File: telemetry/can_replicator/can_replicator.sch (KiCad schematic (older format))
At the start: 34 parts, among them J1 CONN_02X03, J2 MM_M_VT_20, U1 MCP2561-E_SN, U2 ATMEGA16M1, U3 USB_MicroB, U4 FT232RL, Y1 Crystal_SMD

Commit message: fix: fixes based on review checklist
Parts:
- added D7: BAT400D-7-F, footprints:SOT-23-3_OEM, symbol formula:BAT400D-7-F
- added F1: F_500mA_16V, footprints:Fuse_1210, symbol formula:F_500mA_16V
- added U5, U6: R_500, footprints:R_0805_OEM, symbol formula:R_500
- C1, C2: symbol template-rescue:C_0.1uF-formula -> formula:C_0.1uF
- C3: symbol template-rescue:C_100pF-formula -> formula:C_100pF
- C4, C5: symbol template-rescue:C_30pF-formula -> formula:C_30pF
- J1: symbol template-rescue:CONN_02X03-formula -> formula:CONN_02X03
- R1: symbol template-rescue:R_100-formula -> formula:R_100
- R3: symbol template-rescue:R_10K-formula -> formula:R_10K
- U1: symbol template-rescue:MCP2561-E_SN-formula -> formula:MCP2561-E_SN
- Y1: symbol template-rescue:Crystal_SMD-formula -> formula:Crystal_SMD
- gave numbers to parts that had none: 1
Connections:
- net labels added: +5V
- net labels removed: VCC
- wire segments 95 -> 102
- no-connect marks 30 -> 32
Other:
- note added: "+4.4V - +5.25V"
- moved on the sheet: C6, C7, C8, C9, D8, TP2, U4

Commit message: fix: cleanup schematic based on DR feedback
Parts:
- removed J2: MM_M_VT_20, footprints:micromatch_female_vert_20, symbol formula:MM_M_VT_20
- added J?: MM_M_VT_20, footprints:micromatch_female_ra_20, symbol formula:MM_M_VT_20
- renumbered U5 to R10, U6 to R11
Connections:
- net CAN_+: now also J?.3
- net CAN_-: now also J?.4
- net GND: now also J?.1, J?.10, J?.11, J?.12, J?.13, J?.14, J?.15, J?.16, J?.17, J?.18, J?.19, J?.20, J?.5, J?.6, J?.7, J?.8, J?.9
- net USB_RXD renamed UART_RXD
- net USB_TXD renamed UART_TXD
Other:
- note added: "CONNECTOR"
- moved on the sheet: C6, D1, D2, D3, D4, D5, D6, J1, R4, R5, R6, R7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

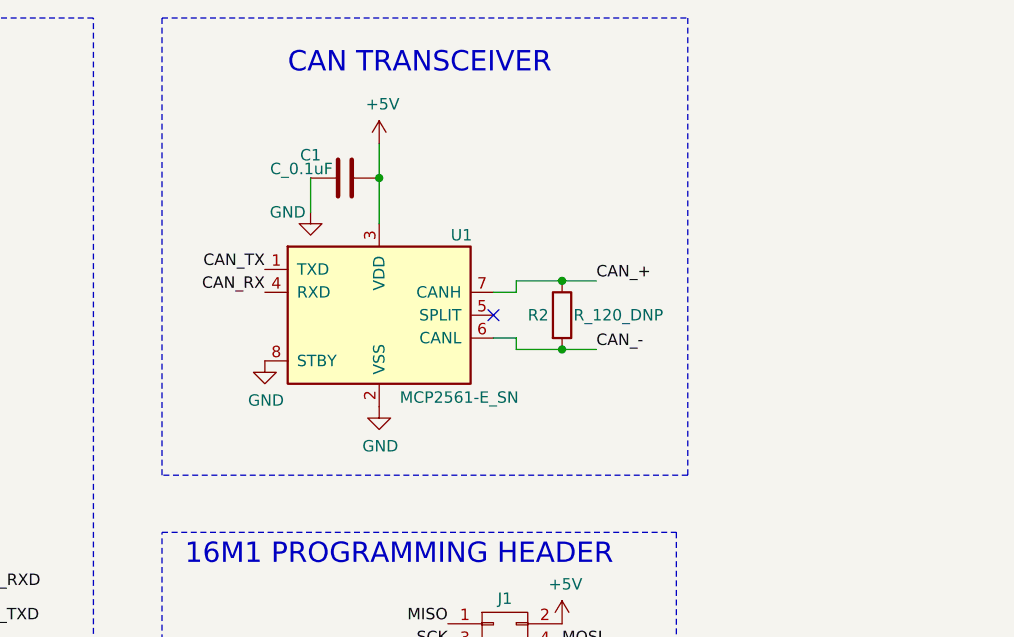
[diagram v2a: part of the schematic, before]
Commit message: feat: add terminating resistors for CAN bus with jumpers
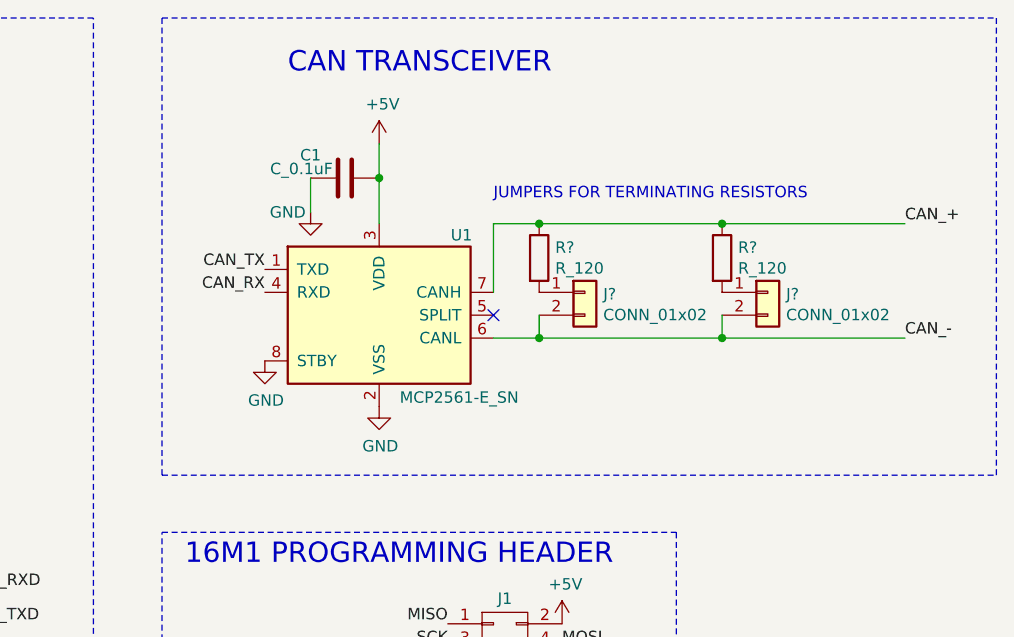
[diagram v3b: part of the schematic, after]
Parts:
- removed R2: R_120_DNP, footprints:R_0805_OEM, symbol formula:R_120_DNP
- added J? (x2): CONN_01x02, Connector_PinHeader_2.54mm:PinHeader_1x02_P2.54mm_Vertical, symbol formula:CONN_01x02
- added R? (x2): R_120, footprints:R_0805_OEM, symbol formula:R_120
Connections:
- net CAN_+: now also R?.1, R?.1
- net CAN_-: now also J?.2 (Pin_2), J?.2 (Pin_2)
- new net: J?.1 (Pin_1), R?.2 (x2)
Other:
- note added: "JUMPERS FOR TERMINATING RESISTORS"
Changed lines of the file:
@@
 Text Label 5850 2200 2    50   ~ 0
 CAN_RX
-Text Label 7300 2150 0    50   ~ 0
+Text Label 8650 1900 0    50   ~ 0
 CAN_+
-Text Label 7300 2450 0    50   ~ 0
+Text Label 8650 2400 0    50   ~ 0
 CAN_-
 Text Notes 2550 1250 0    89   ~ 0
@@
 Wire Wire Line
 	6350 1700 6350 1550
-Wire Wire Line
-	6850 2200 6950 2200
-Wire Wire Line
-	6950 2200 6950 2150
-Wire Wire Line
-	6950 2400 6950 2450
-Wire Wire Line
-	6850 2400 6950 2400
 Text Notes 1800 6050 0    89   ~ 0
 USB + POWER
@@
 	5100 1000 850  1000
 Wire Notes Line
-	5400 1000 7700 1000
-Wire Notes Line
-	7700 1000 7700 3000
-Wire Notes Line
-	7700 3000 5400 3000
+	9050 1000 9050 3000
 Wire Notes Line
 	5400 3000 5400 1000
@@
 	1    0    0    -1
 $EndComp
-Wire Wire Line
-	6950 2150 7150 2150
-Wire Wire Line
-	6950 2450 7150 2450
-$Comp
-L formula:R_120_DNP R2
-U 1 1 5FB3CE18
-P 7150 2300
-F 0 "R2" H 7000 2300 50  0000 L CNN
-F 1 "R_120_DNP" H 7200 2300 50  0000 L CNN
-F 2 "footprints:R_0805_OEM" H 5950 2450 50  0001 L CNN
-F 3 "https://www.mouser.com/datasheet/2/315/AOA0000C304-1149620.pdf" H 5950 2750 50  0001 L CNN
-F 4 "DK" H 7150 2300 60  0001 C CNN "MFN"
-F 5 "667-ERJ-6ENF1200V" H 5950 2550 60  0001 L CNN "MPN"
-F 6 "https://www.mouser.com/ProductDetail/Panasonic-Industrial-Devices/ERJ-6ENF1200V?qs=sGAEpiMZZMvdGkrng054t8AJgcdMkx7x%252bFQnctTMUmU%3d" H 5950 2650 60  0001 L CNN "PurchasingLink"
-	1    7150 2300
-	1    0    0    -1
-$EndComp
-Connection ~ 7150 2150
-Wire Wire Line
-	7150 2150 7300 2150
-Connection ~ 7150 2450
-Wire Wire Line
-	7150 2450 7300 2450
 NoConn ~ 1100 7550
 NoConn ~ 3950 3750
@@
 Text Label 4500 3650 0    50   ~ 0
 UART_TXD
+$Comp
+L formula:CONN_01x02 J?
+U 1 1 604765A9
+P 7250 2200
+F 0 "J?" H 7330 2192 50  0000 L CNN
+F 1 "CONN_01x02" H 7330 2101 50  0000 L CNN
+F 2 "Connector_PinHeader_2.54mm:PinHeader_1x02_P2.54mm_Vertical" H 7150 2200 50  0001 C CNN
+F 3 "https://katalog.we-online.de/em/datasheet/6130xx11121.pdf" H 7250 2300 50  0001 C CNN
+F 4 "DK" H 7350 2400 50  0001 C CNN "MFN"
+F 5 "732-5315-ND" H 7450 2500 50  0001 C CNN "MPN"
+	1    7250 2200
+	1    0    0    -1
+$EndComp
+Wire Wire Line
+	6850 2400 7050 2400
+Wire Wire Line
+	7050 2300 7050 2400
+Connection ~ 7050 2400
+Wire Wire Line
+	7050 2400 7850 2400
+$Comp
+L formula:R_120 R?
+U 1 1 604A0174
+P 7050 2050
+F 0 "R?" H 7120 2096 50  0000 L CNN
+F 1 "R_120" H 7120 2005 50  0000 L CNN
+F 2 "footprints:R_0805_OEM" H 5850 2200 50  0001 L CNN
+F 3 "https://www.mouser.com/datasheet/2/315/AOA0000C304-1149620.pdf" H 5850 2500 50  0001 L CNN
+F 4 "DK" H 7050 2050 60  0001 C CNN "MFN"
+F 5 "667-ERJ-6ENF1200V" H 5850 2300 60  0001 L CNN "MPN"
+F 6 "https://www.mouser.com/ProductDetail/Panasonic-Industrial-Devices/ERJ-6ENF1200V?qs=sGAEpiMZZMvdGkrng054t8AJgcdMkx7x%252bFQnctTMUmU%3d" H 5850 2400 60  0001 L CNN "PurchasingLink"
+	1    7050 2050
+	1    0    0    -1
+$EndComp
+Wire Wire Line
+	6850 2200 6850 1900
+Wire Wire Line
+	6850 1900 7050 1900
+Connection ~ 7050 1900
+Wire Wire Line
+	7050 1900 7850 1900
+$Comp
+L formula:CONN_01x02 J?
+U 1 1 604B1E63
+P 8050 2200
+F 0 "J?" H 8130 2192 50  0000 L CNN
+F 1 "CONN_01x02" H 8130 2101 50  0000 L CNN
+F 2 "Connector_PinHeader_2.54mm:PinHeader_1x02_P2.54mm_Vertical" H 7950 2200 50  0001 C CNN
+F 3 "https://katalog.we-online.de/em/datasheet/6130xx11121.pdf" H 8050 2300 50  0001 C CNN
+F 4 "DK" H 8150 2400 50  0001 C CNN "MFN"
+F 5 "732-5315-ND" H 8250 2500 50  0001 C CNN "MPN"
+	1    8050 2200
+	1    0    0    -1
+$EndComp
+Wire Wire Line
+	7850 2300 7850 2400
+$Comp
+L formula:R_120 R?
+U 1 1 604B2391
+P 7850 2050
+F 0 "R?" H 7920 2096 50  0000 L CNN
+F 1 "R_120" H 7920 2005 50  0000 L CNN
+F 2 "footprints:R_0805_OEM" H 6650 2200 50  0001 L CNN
+F 3 "https://www.mouser.com/datasheet/2/315/AOA0000C304-1149620.pdf" H 6650 2500 50  0001 L CNN
+F 4 "DK" H 7850 2050 60  0001 C CNN "MFN"
+F 5 "667-ERJ-6ENF1200V" H 6650 2300 60  0001 L CNN "MPN"
+F 6 "https://www.mouser.com/ProductDetail/Panasonic-Industrial-Devices/ERJ-6ENF1200V?qs=sGAEpiMZZMvdGkrng054t8AJgcdMkx7x%252bFQnctTMUmU%3d" H 6650 2400 60  0001 L CNN "PurchasingLink"
+	1    7850 2050
+	1    0    0    -1
+$EndComp
+Connection ~ 7850 1900
+Connection ~ 7850 2400
+Wire Wire Line
+	7850 2400 8650 2400
+Wire Wire Line
+	7850 1900 8650 1900
+Wire Notes Line
+	5400 3000 9050 3000
+Wire Notes Line
+	5400 1000 9050 1000
+Text Notes 6850 1800 0    50   ~ 0
+JUMPERS FOR TERMINATING RESISTORS
 $EndSCHEMATC

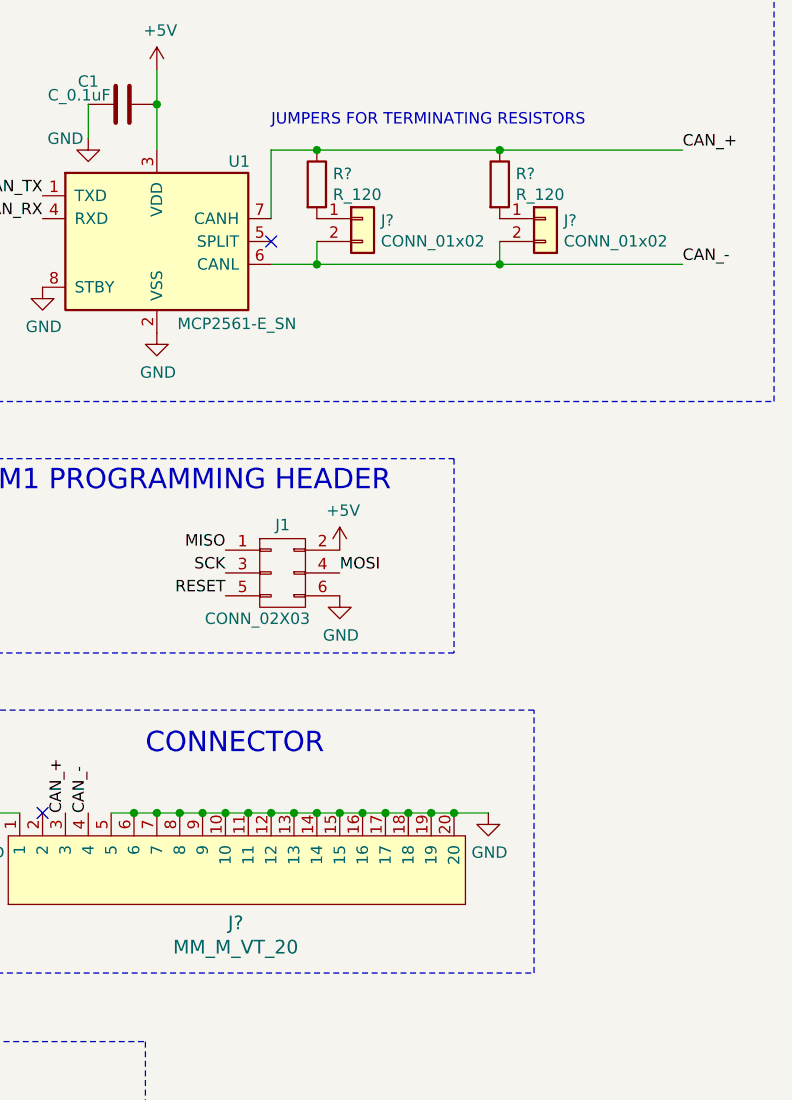
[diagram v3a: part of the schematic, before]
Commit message: chore: annotate symbols and assign footprints
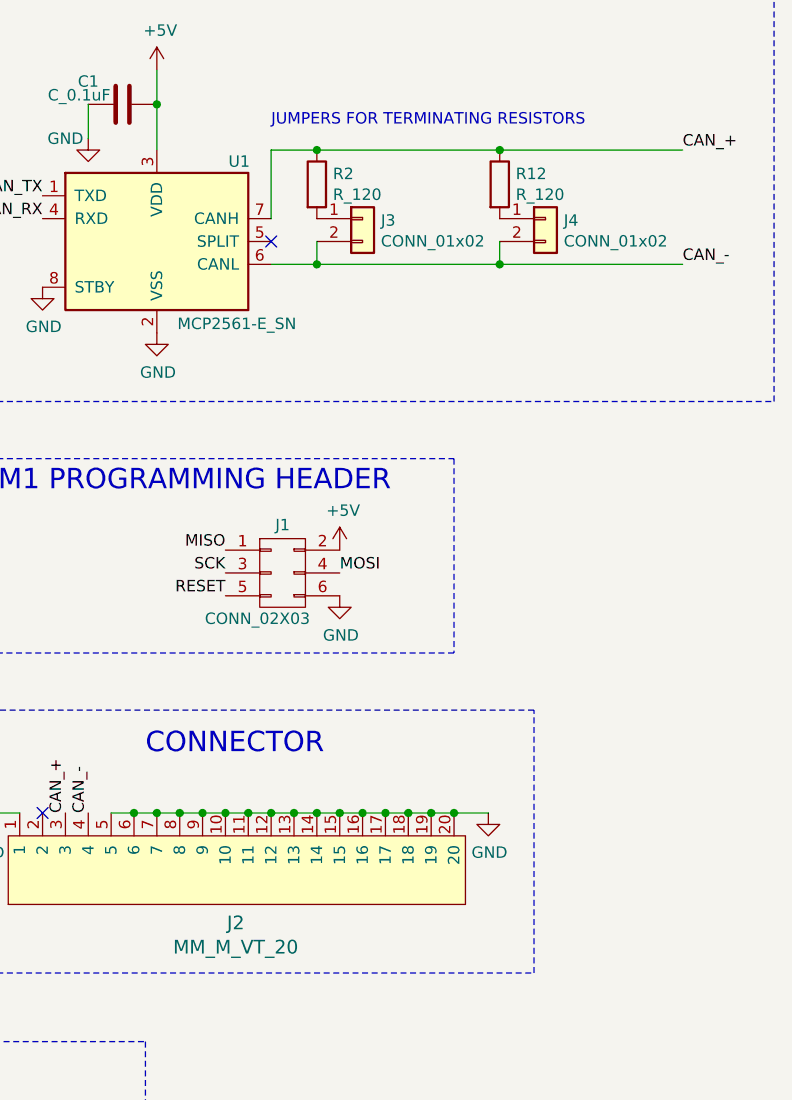
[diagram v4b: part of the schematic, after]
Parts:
- gave numbers to parts that had none: 5
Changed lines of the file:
@@
 STATUS LEDS
 $Comp
-L formula:MM_M_VT_20 J?
+L formula:MM_M_VT_20 J2
 U 1 1 60394CE9
 P 6850 4950
-F 0 "J?" V 6519 5105 60  0000 C CNN
+F 0 "J2" V 6519 5105 60  0000 C CNN
 F 1 "MM_M_VT_20" V 6413 5105 60  0000 C CNN
 F 2 "footprints:micromatch_female_ra_20" H 6650 6050 60  0001 C CNN
@@
 	7650 4800 7800 4800
 $Comp
-L power:GND #PWR?
+L power:GND #PWR020
 U 1 1 6039EEAA
 P 7800 4800
-F 0 "#PWR?" H 7800 4550 50  0001 C CNN
+F 0 "#PWR020" H 7800 4550 50  0001 C CNN
 F 1 "GND" H 7805 4627 50  0000 C CNN
 F 2 "" H 7800 4800 50  0001 C CNN
@@
 $EndComp
 $Comp
-L power:GND #PWR?
+L power:GND #PWR019
 U 1 1 6039FA95
 P 5600 4800
-F 0 "#PWR?" H 5600 4550 50  0001 C CNN
+F 0 "#PWR019" H 5600 4550 50  0001 C CNN
 F 1 "GND" H 5605 4627 50  0000 C CNN
 F 2 "" H 5600 4800 50  0001 C CNN
@@
 UART_TXD
 $Comp
-L formula:CONN_01x02 J?
+L formula:CONN_01x02 J3
 U 1 1 604765A9
 P 7250 2200
-F 0 "J?" H 7330 2192 50  0000 L CNN
+F 0 "J3" H 7330 2192 50  0000 L CNN
 F 1 "CONN_01x02" H 7330 2101 50  0000 L CNN
 F 2 "Connector_PinHeader_2.54mm:PinHeader_1x02_P2.54mm_Vertical" H 7150 2200 50  0001 C CNN
@@
 	7050 2400 7850 2400
 $Comp
-L formula:R_120 R?
+L formula:R_120 R2
 U 1 1 604A0174
 P 7050 2050
-F 0 "R?" H 7120 2096 50  0000 L CNN
+F 0 "R2" H 7120 2096 50  0000 L CNN
 F 1 "R_120" H 7120 2005 50  0000 L CNN
 F 2 "footprints:R_0805_OEM" H 5850 2200 50  0001 L CNN
@@
 	7050 1900 7850 1900
 $Comp
-L formula:CONN_01x02 J?
+L formula:CONN_01x02 J4
 U 1 1 604B1E63
 P 8050 2200
-F 0 "J?" H 8130 2192 50  0000 L CNN
+F 0 "J4" H 8130 2192 50  0000 L CNN
 F 1 "CONN_01x02" H 8130 2101 50  0000 L CNN
 F 2 "Connector_PinHeader_2.54mm:PinHeader_1x02_P2.54mm_Vertical" H 7950 2200 50  0001 C CNN
@@
 	7850 2300 7850 2400
 $Comp
-L formula:R_120 R?
+L formula:R_120 R12
 U 1 1 604B2391
 P 7850 2050
-F 0 "R?" H 7920 2096 50  0000 L CNN
+F 0 "R12" H 7920 2096 50  0000 L CNN
 F 1 "R_120" H 7920 2005 50  0000 L CNN
 F 2 "footprints:R_0805_OEM" H 6650 2200 50  0001 L CNN

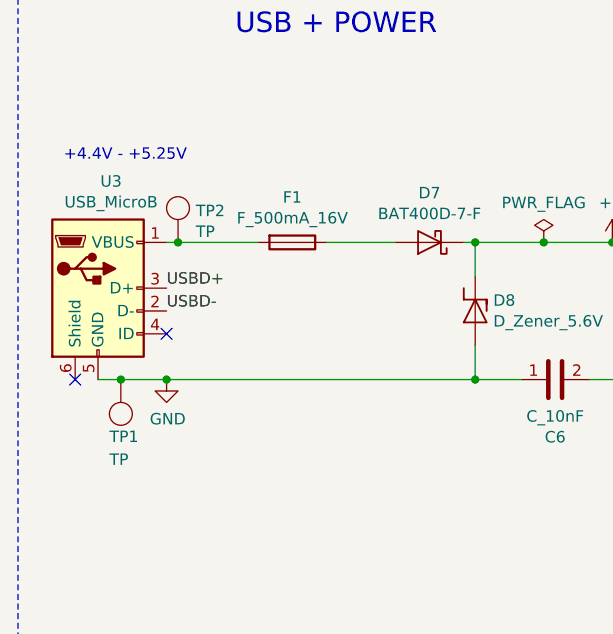
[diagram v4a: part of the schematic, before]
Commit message: fix: replace test points with SMD
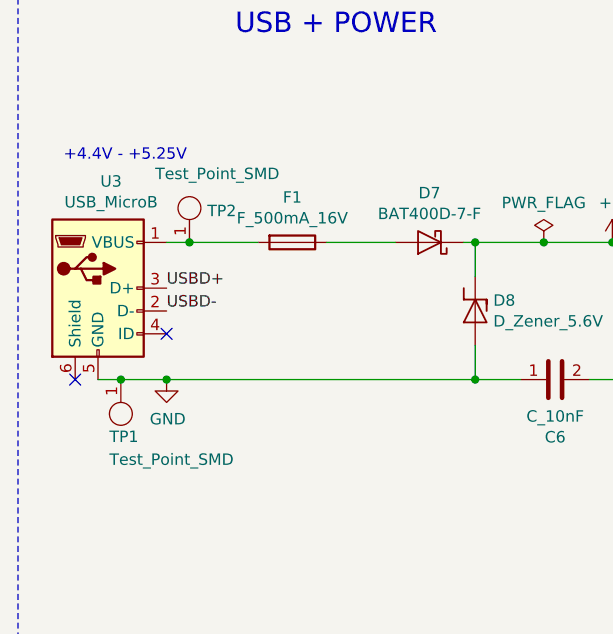
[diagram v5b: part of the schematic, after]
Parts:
- removed TP1, TP2: TP, footprints:tp_1.6mm, symbol formula:TP
- added TP1, TP2: Test_Point_SMD, footprints:Test_Point_SMD, symbol formula:Test_Point_SMD
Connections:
- net GND: now also TP1.1
- net at F1.2, U3.1 (VBUS): now also TP2.1
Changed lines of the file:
@@
 	1    0    0    -1
 $EndComp
-Wire Wire Line
-	1200 7550 1300 7550
 $Comp
 L formula:USB_MicroB U3
@@
 NoConn ~ 3950 1950
 Wire Wire Line
-	1500 6950 1550 6950
-Wire Wire Line
 	4450 6250 4800 6250
 Wire Wire Line
@@
 Wire Notes Line
 	5400 3250 7650 3250
-$Comp
-L formula:TP TP2
-U 1 1 5FCAB95B
-P 1550 6750
-F 0 "TP2" H 1628 6688 50  0000 L CNN
-F 1 "TP" H 1628 6597 50  0000 L CNN
-F 2 "footprints:tp_1.6mm" H 1450 6650 50  0001 C CNN
-F 3 "http://www.keyelco.com/product-pdf.cfm?p=1314" H 1550 6750 50  0001 C CNN
-F 4 "DK" H 1650 6850 50  0001 C CNN "MFN"
-F 5 "36-5006-ND" H 1750 6950 50  0001 C CNN "MPN"
-F 6 "https://www.digikey.com/product-detail/en/keystone-electronics/5006/36-5006-ND/255330" H 1850 7050 50  0001 C CNN "PurchasingLink"
-	1    1550 6750
-	1    0    0    -1
-$EndComp
-$Comp
-L formula:TP TP1
-U 1 1 5FCB51EF
-P 1300 7750
-F 0 "TP1" H 1350 7800 50  0000 R CNN
-F 1 "TP" H 1350 7900 50  0000 R CNN
-F 2 "footprints:tp_1.6mm" H 1200 7650 50  0001 C CNN
-F 3 "http://www.keyelco.com/product-pdf.cfm?p=1314" H 1300 7750 50  0001 C CNN
-F 4 "DK" H 1400 7850 50  0001 C CNN "MFN"
-F 5 "36-5006-ND" H 1500 7950 50  0001 C CNN "MPN"
-F 6 "https://www.digikey.com/product-detail/en/keystone-electronics/5006/36-5006-ND/255330" H 1600 8050 50  0001 C CNN "PurchasingLink"
-	1    1300 7750
-	-1   0    0    1
-$EndComp
-Connection ~ 1300 7550
-Wire Wire Line
-	1300 7550 1500 7550
 $Comp
 L formula:D_Zener_5.6V D8
@@
 $EndComp
 Wire Wire Line
-	1900 6950 1550 6950
-Connection ~ 1550 6950
-Wire Wire Line
 	2200 6950 2500 6950
 Wire Wire Line
@@
 Text Notes 6850 1800 0    50   ~ 0
 JUMPERS FOR TERMINATING RESISTORS
+$Comp
+L formula:Test_Point_SMD TP2
+U 1 1 6052D1D7
+P 1600 6900
+F 0 "TP2" H 1678 6988 50  0000 L CNN
+F 1 "Test_Point_SMD" H 1450 7150 50  0000 L CNN
+F 2 "footprints:Test_Point_SMD" H 1600 6750 50  0001 C CNN
+F 3 "" H 1600 6900 50  0001 C CNN
+	1    1600 6900
+	1    0    0    -1
+$EndComp
+Wire Wire Line
+	1500 6950 1600 6950
+Connection ~ 1600 6950
+Wire Wire Line
+	1600 6950 1900 6950
+Wire Wire Line
+	1200 7550 1300 7550
+$Comp
+L formula:Test_Point_SMD TP1
+U 1 1 6052ED64
+P 1300 7600
+F 0 "TP1" H 1350 7800 50  0000 R CNN
+F 1 "Test_Point_SMD" H 1350 7900 50  0000 R CNN
+F 2 "footprints:Test_Point_SMD" H 1300 7450 50  0001 C CNN
+F 3 "" H 1300 7600 50  0001 C CNN
+	1    1300 7600
+	-1   0    0    1
+$EndComp
+Connection ~ 1300 7550
+Wire Wire Line
+	1300 7550 1500 7550
 $EndSCHEMATC
